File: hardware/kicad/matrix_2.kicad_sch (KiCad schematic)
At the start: 142 parts, among them U6 IS31FL3741A

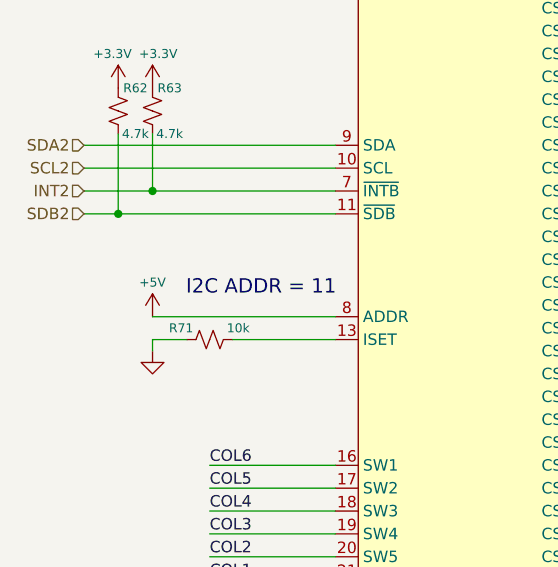
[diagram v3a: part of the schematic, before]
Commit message: esp32c3 upgrade, route usb, fix errors
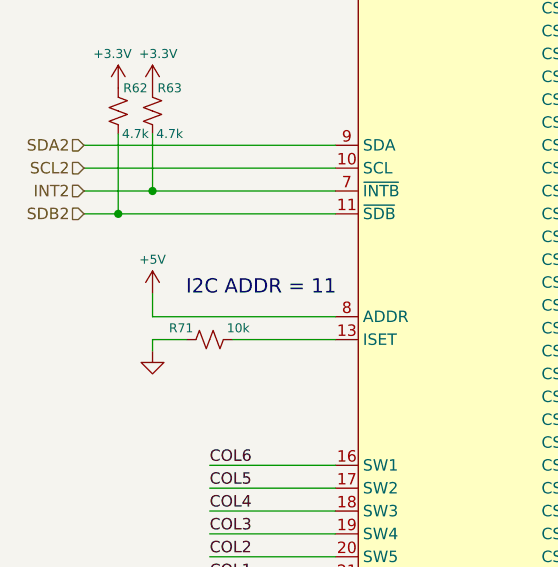
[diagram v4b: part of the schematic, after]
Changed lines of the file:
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@@
 	(wire
 		(pts
+			(xy 40.64 97.79) (xy 60.96 97.79)
+		)
+		(stroke
+			(width 0)
+			(type default)
+		)
+	)
+	(wire
+		(pts
 			(xy 222.25 146.05) (xy 222.25 144.78)
 		)
@@
 	(wire
 		(pts
+			(xy 40.64 95.25) (xy 40.64 97.79)
+		)
+		(stroke
+			(width 0)
+			(type default)
+		)
+	)
+	(wire
+		(pts
 			(xy 222.25 245.11) (xy 223.52 245.11)
 		)
@@
 	(wire
 		(pts
-			(xy 40.64 97.79) (xy 60.96 97.79)
-		)
-		(stroke
-			(width 0)
-			(type default)
-		)
-	)
-	(wire
-		(pts
 			(xy 139.7 222.25) (xy 146.05 222.25)
 		)
@@
 	(symbol
 		(lib_id "power:+5V")
-		(at 40.64 97.79 0)
+		(at 40.64 95.25 0)
 		(unit 1)
 		(exclude_from_sim no)
@@
 		(dnp no)
 		(property "Reference" "#PWR031"
-			(at 40.64 101.6 0)
+			(at 40.64 99.06 0)
 			(effects
 				(font
@@
 		)
 		(property "Value" "+5V"
-			(at 40.64 93.98 0)
+			(at 40.64 91.44 0)
 			(effects
 				(font
@@
 		)
 		(property "Footprint" ""
-			(at 40.64 97.79 0)
+			(at 40.64 95.25 0)
 			(effects
 				(font
@@
 		)
 		(property "Datasheet" ""
-			(at 40.64 97.79 0)
+			(at 40.64 95.25 0)
 			(effects
 				(font
@@
 		)
 		(property "Description" "Power symbol creates a global label with name \"+5V\""
-			(at 40.64 97.79 0)
+			(at 40.64 95.25 0)
 			(effects
 				(font
